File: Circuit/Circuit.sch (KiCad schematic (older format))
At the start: 22 parts, among them J1 UE27AC54100, J2 22-23-2021, J3 22-23-2021, J4 22-23-2021, Q1 AO3401A, Q2 2N2222A, U1 L4978

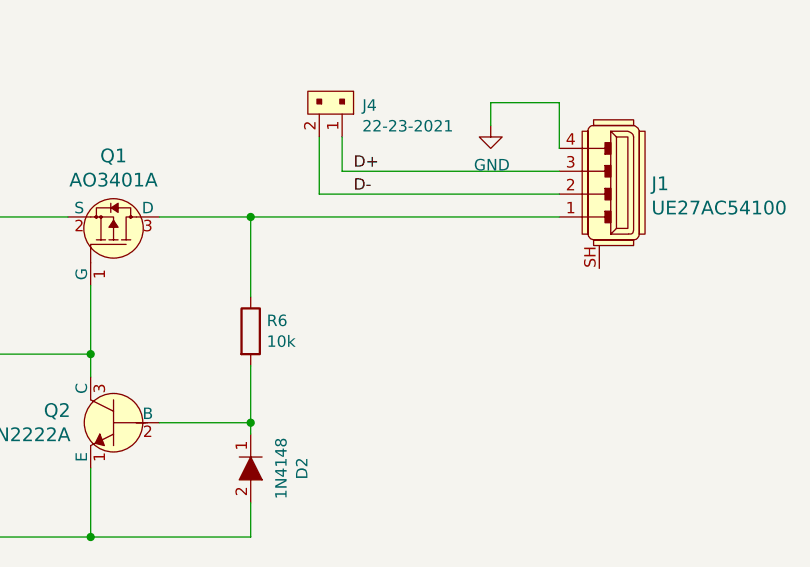
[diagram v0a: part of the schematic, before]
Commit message: Soon finnished with PCB
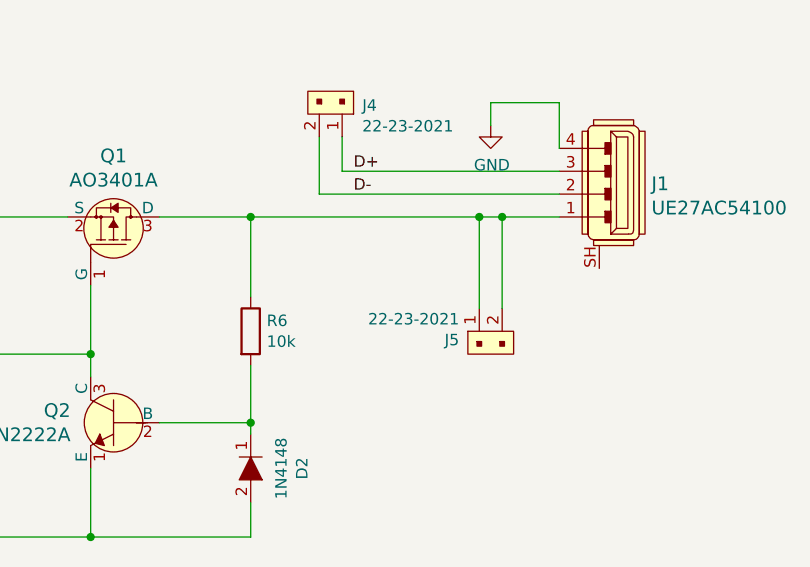
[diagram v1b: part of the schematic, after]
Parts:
- added J5: 22-23-2021, digikey-footprints:PinHeader_1x2_P2.54mm_Drill1.02mm, symbol dk_Rectangular-Connectors-Headers-Male-Pins:22-23-2021
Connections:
- net at J1.1, Q1.3 (D), R6.1: now also J5.1, J5.2
